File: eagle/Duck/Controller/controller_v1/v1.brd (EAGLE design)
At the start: 100 x 100 mm, 8 parts

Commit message: Upside down
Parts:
- moved R1 64.0 mm to (42.0, 79.0)
- moved R2 49.1 mm to (37.0, 79.0)
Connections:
- removed net 16: U$3.16, U$4.P$1
- removed net 17: U$3.17, U$5.P$1
- removed net 34: R1.1, U$3.34
- removed net 35: R2.1, U$3.35
- new net LED1: R1.1, U$3.14
- new net LED2: R2.1, U$3.13
- new net SW1: U$3.35, U$4.P$1
- new net SW2: U$3.27, U$5.P$1
- net RS: now also U$3.26; no longer U$3.2
- net RST: now also U$3.25; no longer U$3.4
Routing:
- net GND: track 0.00 -> 256.9 mm
- net CS: track 0.00 -> 179.8 mm
- net +3V3: track 0.00 -> 170.2 mm
- net SDA: track 0.00 -> 113.0 mm
- net CLK: track 0.00 -> 88.7 mm
- net RST: track 0.00 -> 76.2 mm
- net RS: track 0.00 -> 68.3 mm
- net SW2: track 0.00 -> 60.9 mm
- net LED2: track 0.00 -> 51.9 mm
- net CN12: track 0.00 -> 49.1 mm
- net CN15: track 0.00 -> 48.2 mm
- net N$4: track 0.00 -> 44.7 mm
- net LED1: track 0.00 -> 40.5 mm
- net SW1: track 0.00 -> 36.6 mm
- net I2C_SDA: track 0.00 -> 22.3 mm
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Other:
- outline, holes or cut-outs redrawn

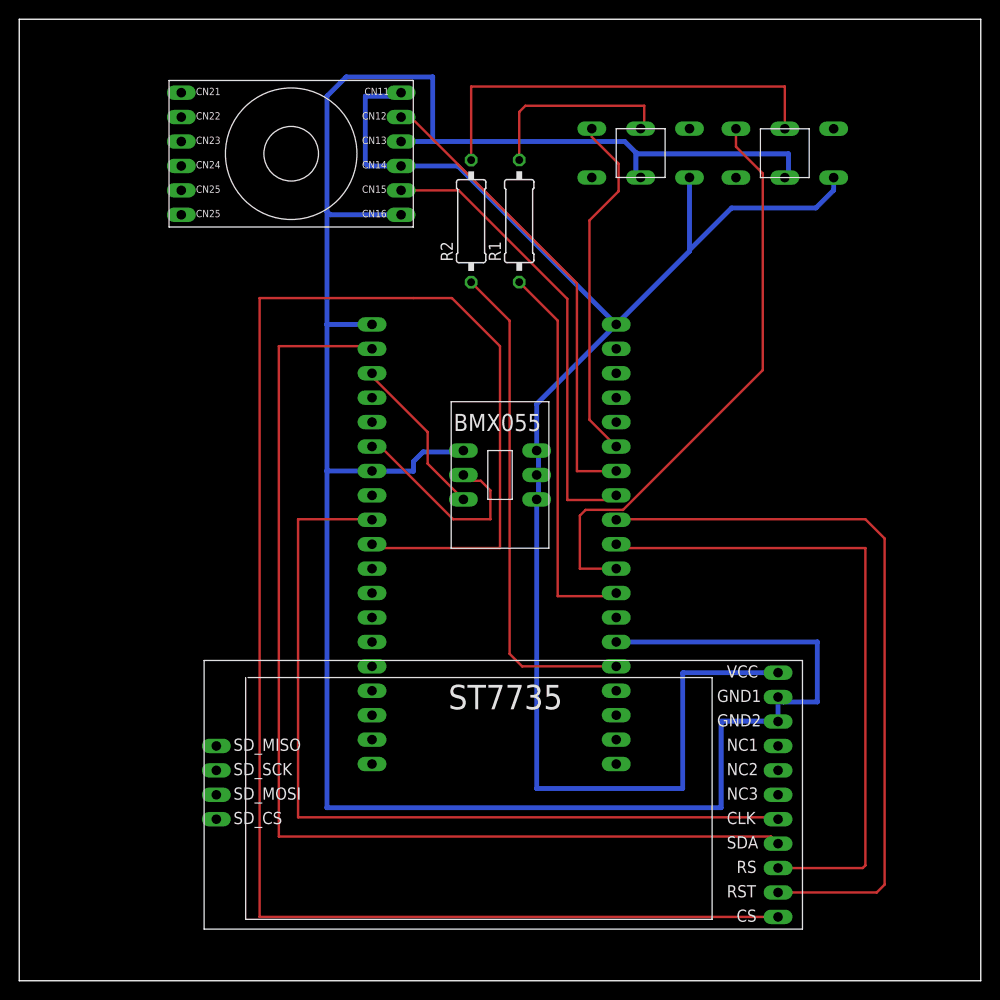
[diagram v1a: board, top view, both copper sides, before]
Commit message: wiring finished
but  refactoring needed.
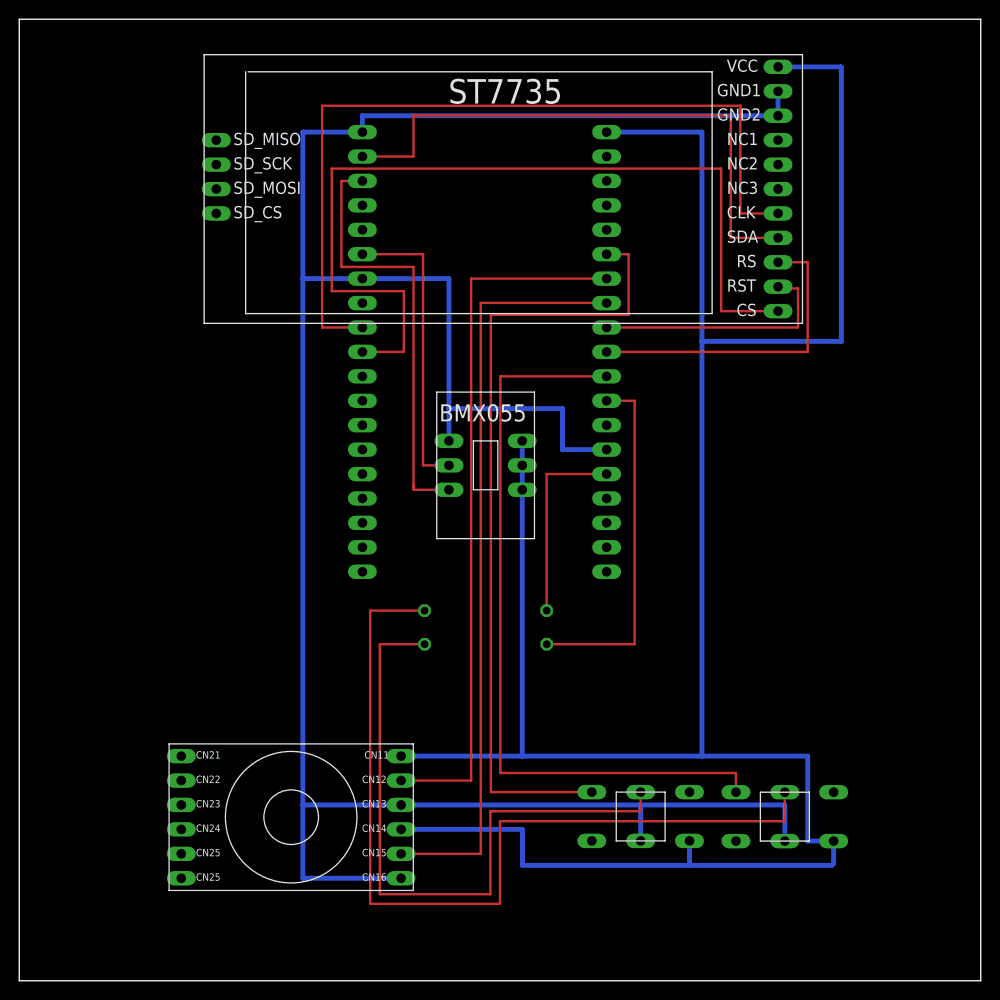
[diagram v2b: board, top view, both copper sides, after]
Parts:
- moved U$2 69.0 mm to (10.7, 20.8)
- moved U$4 69.0 mm to (47.0, 12.0)
- moved U$5 69.0 mm to (62.0, 12.0)
- moved U$1 63.0 mm to (68.9, 83.6)
- moved R1 44.1 mm to (38.5, 35.0), flipped to the bottom, turned to 0 degrees
- moved R2 40.5 mm to (38.5, 38.5), flipped to the bottom, turned to 0 degrees
- moved U$3 20.0 mm to (51.1, 88.3)
- moved U$6 1.80 mm to (38.5, 56.1)
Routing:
- net +3V3: track 170.2 -> 264.7 mm
- net CS: track 179.8 -> 92.1 mm
- net SDA: track 113.0 -> 60.2 mm
- net RST: track 76.2 -> 26.1 mm
- net N$3: track 20.8 -> 68.4 mm
- net SW1: track 36.6 -> 83.1 mm
- net N$4: track 44.7 -> 90.9 mm
- net RS: track 68.3 -> 33.3 mm
- net LED2: track 51.9 -> 20.4 mm
- net CN15: track 48.2 -> 78.7 mm
- net I2C_SCL: track 17.1 -> 45.5 mm
- net CN12: track 49.1 -> 73.6 mm
- net SW2: track 60.9 -> 78.8 mm
- net I2C_SDA: track 22.3 -> 31.0 mm
- net GND: track 256.9 -> 251.8 mm
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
